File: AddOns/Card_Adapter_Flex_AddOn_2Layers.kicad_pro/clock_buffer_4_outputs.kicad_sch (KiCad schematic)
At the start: 12 parts, among them U1 5PB1214CMGK8

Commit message: .
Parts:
- U1: value 5PB1214CMGK8 -> 5PB1214
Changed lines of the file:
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@@
 			)
 		)
-		(property "Value" "5PB1214CMGK8"
+		(property "Value" "5PB1214"
 			(at 142.24 82.55 0)
 			(effects

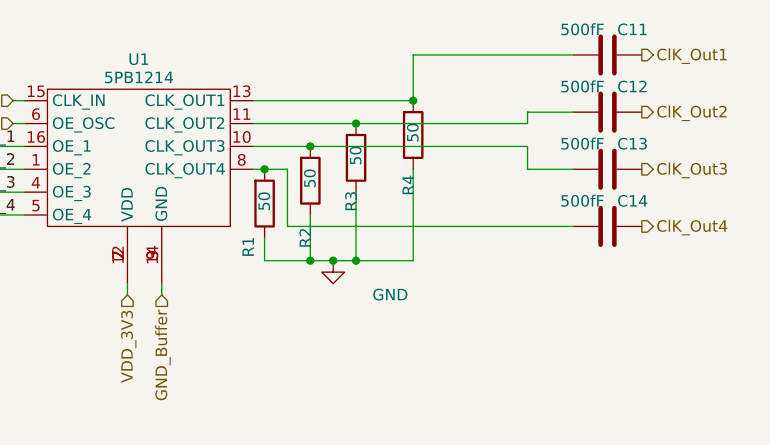
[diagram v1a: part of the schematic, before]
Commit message: Update PCB layout and net assignments for new capacitors
Added new nets and updated net assignments for several capacitors (C11, C12, C13, C14, C18, C19, C20, C21) in the PCB layout. Modified footprints, positions, and values for various components including resistors and capacitors. Updated backup files and added a lock file for the project.
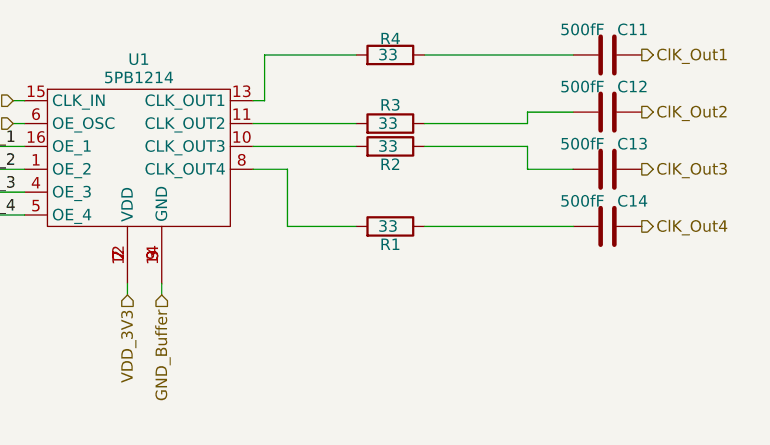
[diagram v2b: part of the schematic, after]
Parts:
- R1, R2, R3, R4: value 50 -> 33
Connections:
- net GND: no longer R1.1, R2.1, R3.1, R4.1
- net at R4.2, U1.13 (CLK_OUT1): no longer C11.2
- net at R2.2, U1.10 (CLK_OUT3): no longer C13.2
- net at R3.2, U1.11 (CLK_OUT2): no longer C12.2
- net at R1.2, U1.8 (CLK_OUT4): no longer C14.2
- new net: C11.2, R4.1
- new net: C13.2, R2.1
- new net: C12.2, R3.1
- new net: C14.2, R1.1
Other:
- moved on the sheet: R1, R2, R3, R4

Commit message: .
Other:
- note added: "NOTE: 1. One decoupling capacitor per VDD pin 2. Do not share GND of the capacitor with the IC one"
- note removed: "one decoupling capacitor per VDD pin"
- moved on the sheet: C1, C11, C12, C13, C14, C2, C3, R1, R2, R3, R4, U1
